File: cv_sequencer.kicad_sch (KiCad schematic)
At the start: 66 parts, among them J1 4005_SWD_Header, J2 3086_Connector_Eurorack_Power, J3 3096_USBC_RA_SMD, SW1 RST, SW2 BOOTSEL, U1 3097_TFT_Display_SPI, U2 4002_RP2040, U3 4015_Adjustable_Reg_500mA_SOT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, U4 4015_Adjustable_Reg_500mA_SOT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, Y1 4004-Crystal-12MHz_GND24

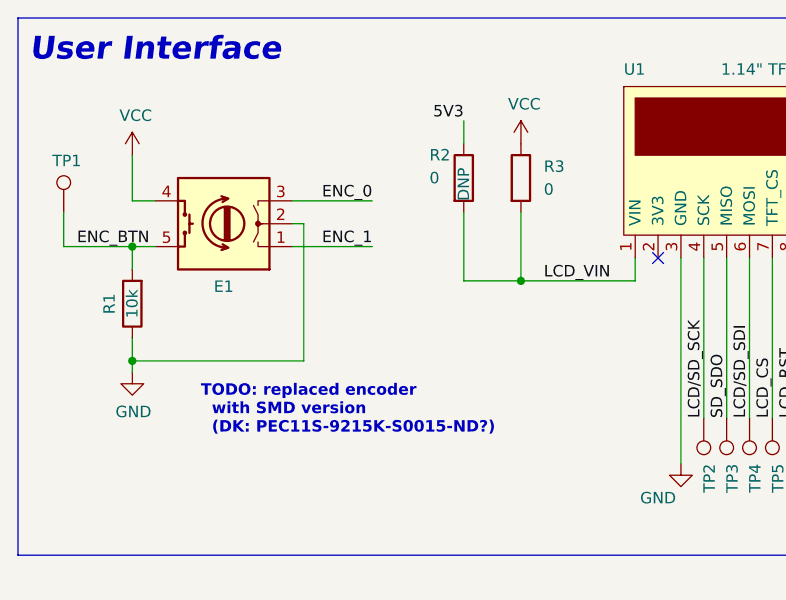
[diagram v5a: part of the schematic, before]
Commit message: Changed encoder to SMD version
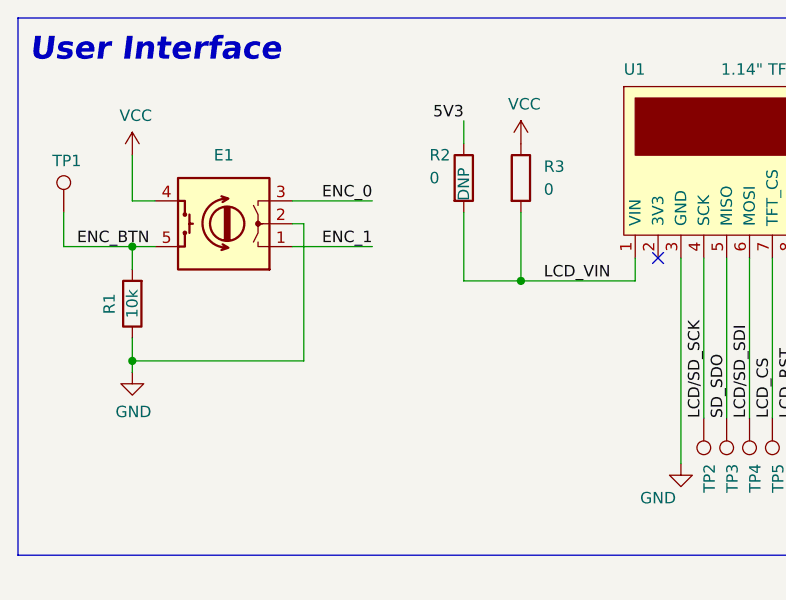
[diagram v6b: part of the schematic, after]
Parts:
- removed E1: 3094_Encoder_Switch, Shulltronics_ElectroMechanical:3094_Encoder_PEC11R, symbol Shulltronics_ElectroMechanical:3094_Encoder_Switch
- added E1: 4025_Encoder_Switch_SMD, Shulltronics_ElectroMechanical:4025_Encoder_PEC11S, symbol Shulltronics_ElectroMechanical:4025_Encoder_Switch_SMD
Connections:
- net ENC_0: now also E1.3
- net ENC_1: now also E1.1
- net ENC_BTN: now also E1.5
- net GND: now also E1.2
- net VCC: now also E1.4
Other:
- note removed: "TODO: replaced encoder with SMD version (DK: PEC11S-9215K-S0015-ND?)"
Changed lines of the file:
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@@
     (effects (font (size 1.27 1.27)) (justify left bottom))
-  )
-  (text "TODO: replaced encoder\n  with SMD version\n  (DK: PEC11S-9215K-S0015-ND?)"
-    (at 34.29 60.325 0)
-    (effects (font (size 1.27 1.27) (thickness 0.254) bold) (justify left bottom))
   )
   (text "USB and SWD Connectors" (at 212.09 90.17 0)
@@
     (pin "5")
   )
+  (symbol (lib_id "Shulltronics_ElectroMechanical:4025_Encoder_Switch_SMD") (at 36.83 36.83 180) (unit 1)
+    (in_bom yes) (on_board yes) (fields_autoplaced)
+    (property "Reference" "E1" (id 0) (at 36.83 29.21 0))
+    (property "Value" "4025_Encoder_Switch_SMD" (id 1) (at 36.83 30.48 0)
+      (effects (font (size 1.27 1.27)) hide)
+    )
+    (property "Footprint" "Shulltronics_ElectroMechanical:4025_Encoder_PEC11S" (id 2) (at 36.83 36.83 0)
+      (effects (font (size 1.27 1.27)) hide)
+    )
+    (property "Datasheet" "https://www.bourns.com/docs/Product-Datasheets/PEC11S.pdf" (id 3) (at 36.83 36.83 0)
+      (effects (font (size 1.27 1.27)) hide)
+    )
+    (property "SPN" "4025" (id 4) (at 36.83 27.94 0)
+      (effects (font (size 1.27 1.27)) hide)
+    )
+    (pin "1")
+    (pin "2")
+    (pin "3")
+    (pin "4")
+    (pin "5")
+  )
   (symbol (lib_id "Shulltronics_Passives:3089_Capacitor_100n_16V_0402") (at 210.82 39.37 90) (unit 1)
     (in_bom yes) (on_board yes)
@@
     (pin "1")
     (pin "2")
-  )
-  (symbol (lib_id "Shulltronics_ElectroMechanical:3094_Encoder_Switch") (at 36.83 36.83 180) (unit 1)
-    (in_bom yes) (on_board yes)
-    (property "Reference" "E1" (id 0) (at 36.83 43.815 0))
-    (property "Value" "3094_Encoder_Switch" (id 1) (at 36.83 30.48 0)
-      (effects (font (size 1.27 1.27)) hide)
-    )
-    (property "Footprint" "Shulltronics_ElectroMechanical:3094_Encoder_PEC11R" (id 2) (at 36.83 36.83 0)
-      (effects (font (size 1.27 1.27)) hide)
-    )
-    (property "Datasheet" "https://www.bourns.com/docs/Product-Datasheets/PEC11R.pdf" (id 3) (at 36.83 36.83 0)
-      (effects (font (size 1.27 1.27)) hide)
-    )
-    (property "SPN" "3094" (id 4) (at 36.83 27.94 0)
-      (effects (font (size 1.27 1.27)) hide)
-    )
-    (pin "1")
-    (pin "2")
-    (pin "3")
-    (pin "4")
-    (pin "5")
   )
   (symbol (lib_id "Shulltronics_Passives:3089_Capacitor_100n_16V_0402") (at 135.89 105.41 0) (unit 1)
@@
       (reference "C26") (unit 1) (value "3089_Capacitor_100n_16V_SMD") (footprint "Shulltronics_Generics:C_0402_HandSolder")
     )
-    (path "/77f076a8-329e-4a40-96ea-5854a454e032"
-      (reference "E1") (unit 1) (value "3094_Encoder_Switch") (footprint "Shulltronics_ElectroMechanical:3094_Encoder_PEC11R")
+    (path "/16a49ecd-abfd-4d6b-abb3-2f90d5cb3b16"
+      (reference "E1") (unit 1) (value "4025_Encoder_Switch_SMD") (footprint "Shulltronics_ElectroMechanical:4025_Encoder_PEC11S")
     )
     (path "/66b30126-0f41-4f28-aeb6-68976a864457"

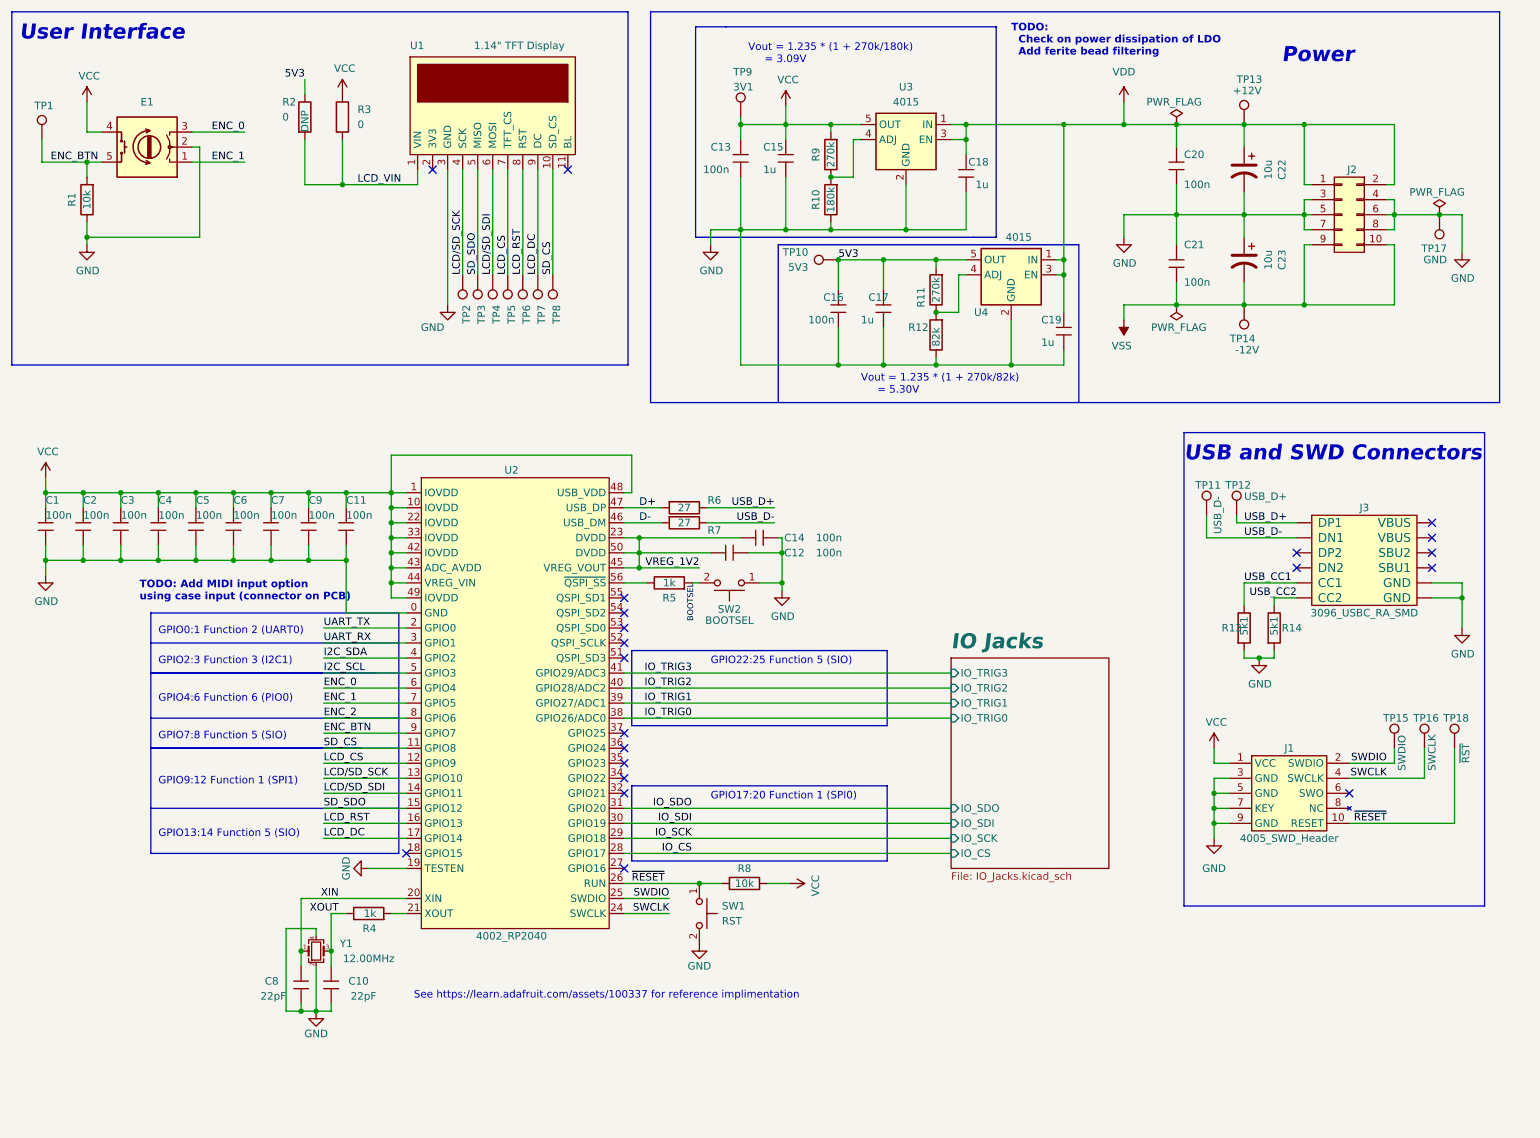
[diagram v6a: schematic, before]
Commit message: gots most components placed nicely, added 4027 for MIDI, still to finish
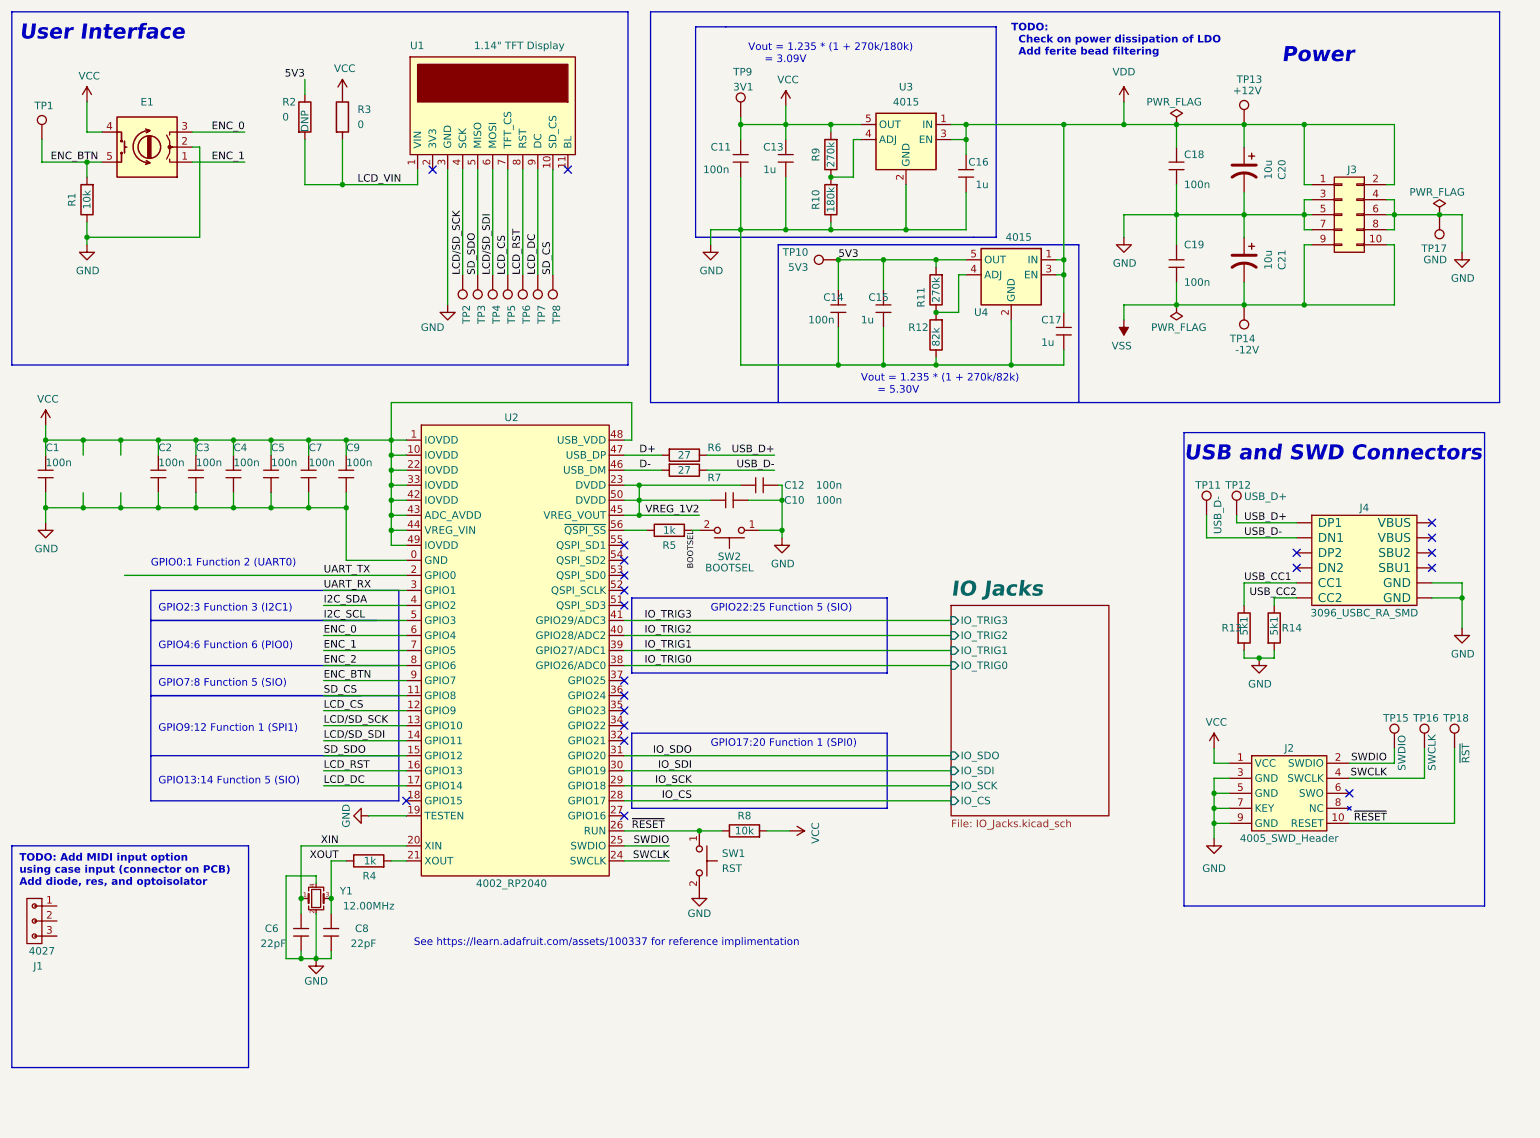
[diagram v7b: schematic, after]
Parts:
- removed C2, C3: 3089_Capacitor_100n_16V_0402, Shulltronics_Generics:C_0402_HandSolder, symbol Shulltronics_Passives:3089_Capacitor_100n_16V_0402
- added J1: 4027_Connector_PicoBlade_3pos_Vert_THT, Shulltronics_Connectors:4027_PicoBlade_3pos_Vert_THT, symbol Shulltronics_Connectors:4027_Connector_PicoBlade_3pos_Vert_THT
- renumbered C12 to C10, C13 to C11, C14 to C12, C15 to C13, C16 to C14, C17 to C15, C18 to C16, C19 to C17, C20 to C18, C21 to C19, C4 to C2, C22 to C20, C23 to C21, C5 to C3, C6 to C4, C7 to C5, C8 to C6, C9 to C7, C10 to C8, C11 to C9, J1 to J2, J2 to J3, J3 to J4
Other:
- note added: "TODO: Add MIDI input option using case input (connector on PCB) Add diode, res, and optoisolator"
- note removed: "TODO: Add MIDI input option using case input (connector on PCB)"
- moved on the sheet: C1, C10, C12, C2, C3, C4, C5, C6, C7, C8, C9, R4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

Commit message: Made minor tweaks, started routing of board
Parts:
- removed C13, C15, C16, C17: 4013_Capacitor_1u_16V_0402, Shulltronics_Generics:C_0402_HandSolder, symbol Shulltronics_Passives:4013_Capacitor_1u_16V_0402
- removed C20, C21: 3088_Capacitor_10u_50V_SMD, Shulltronics_Passives:3088_Capacitor_10u_50V_SMD, symbol Shulltronics_Passives:3088_Capacitor_10u_50V_SMD
- removed J1: 4027_Connector_PicoBlade_3pos_Vert_THT, Shulltronics_Connectors:4027_PicoBlade_3pos_Vert_THT, symbol Shulltronics_Connectors:4027_Connector_PicoBlade_3pos_Vert_THT
- removed R10: 4020_Resistor_SMD_180k_0.125W_1%, Shulltronics_Generics:RES-0402, symbol Shulltronics_Passives:4020_Resistor_SMD_180k_0.125W_1%
- removed R11, R9: 4019_Resistor_SMD_270k_0.125W_1%, Shulltronics_Generics:RES-0402, symbol Shulltronics_Passives:4019_Resistor_SMD_270k_0.125W_1%
- removed R12: 4018_Resistor_SMD_82k_0.125W_1%, Shulltronics_Generics:RES-0402, symbol Shulltronics_Passives:4018_Resistor_SMD_82k_0.125W_1%
- removed U3, U4: 4015_Adjustable_Reg_500mA_SOT-23-5, Shulltronics_Generics:SOT-23-5, symbol Shulltronics_Regulators:4015_Adjustable_Reg_500mA_SOT-23-5
- added C13, C15, C16, C17: 4035_Capacitor_2u2_25V_0402, Shulltronics_Generics:C_0402_HandSolder, symbol Shulltronics_Passives:4035_Capacitor_2u2_25V_0402
- added C20, C21: 4031_Capacitor_10u_35V_SMD, Shulltronics_Passives:3088_Capacitor_10u_50V_SMD, symbol Shulltronics_Passives:4031_Capacitor_10u_35V_SMD
- added J1: 4029_Connector_PicoBlade_4pos_Vert_THT, Shulltronics_Connectors:4029_PicoBlade_4pos_Vert_THT, symbol Shulltronics_Connectors:4029_Connector_PicoBlade_4pos_Vert_THT
- added R10: 4033_Resistor_SMD_18k_0.125W_1%, Shulltronics_Generics:RES-0402, symbol Shulltronics_Passives:4033_Resistor_SMD_18k_0.125W_1%
- added R11, R9: 4016_Resistor_SMD_27k_0.125W_1%, Shulltronics_Generics:RES-0402, symbol Shulltronics_Passives:4016_Resistor_SMD_27k_0.125W_1%
- added R12: 4034_Resistor_SMD_8k2_0.125W_1%, Shulltronics_Generics:RES-0402, symbol Shulltronics_Passives:4034_Resistor_SMD_8k2_0.125W_1%
- added R31, R33: 4030_Resistor_SMD_220_0.125W_1%, Shulltronics_Generics:RES-0402, symbol Shulltronics_Passives:4030_Resistor_SMD_220_0.125W_1%
- added R32: 4008_Resistor_SMD_10k_0.125W_1%, Shulltronics_Generics:RES-0402, symbol Shulltronics_Passives:4008_Resistor_SMD_10k_0.125W_1%
- added U3, U4: 4032_Adjustable_Reg_200mA_SOT-23-5, Shulltronics_Generics:SOT-23-5, symbol Shulltronics_Regulators:4032_Adjustable_Reg_200mA_SOT-23-5
- added U9: 4028_OptoIsolator_TLP290, Shulltronics_Opto:4028_OptoIsolator_TLP290_SOP-4, symbol Shulltronics_Opto:4028_OptoIsolator_TLP290
- J2: SPN (none) -> 4005
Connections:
- net 5V3: now also C15.2, R11.1, U4.5 (OUT)
- net GND: now also C13.1, C15.1, C16.1, C17.1, C20.2, C21.1, R10.2, R12.2, U3.2 (GND), U4.2 (GND), U9.3
- net UART_RX: now also R32.2, U9.4
- net UART_TX: now also J1.3
- net VCC: now also C13.2, R32.1, R33.2, R9.1, U3.5 (OUT)
- net VDD: now also C16.2, C17.2, C20.1, U3.1 (IN), U3.3 (EN), U4.1 (IN), U4.3 (EN)
- net VSS: now also C21.2
- net XOUT: now also R4.2, U2.21 (XOUT); no longer C8.2, R4.1, Y1.3
- new net: R11.2, R12.1, U4.4 (ADJ)
- new net: C8.2, R4.1, Y1.3
- new net: R10.1, R9.2, U3.4 (ADJ)
- new net MIDI_OUT_SRC: J1.4, R33.1
- new net MIDI_R: R31.1, U9.2
- new net MIDI_SNK: J1.1, R31.2
- new net MIDI_SRC: J1.2, U9.1
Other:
- sheet IO Jacks ports: added IO_5V3; removed none
- note added: "MIDI IO"
- note added: "See https://learn.adafruit.com/assets/100337 for RP2040 reference implimentation"
- note added: "TODO: Add PWR and STAT LEDs"
- note added: "TODO: Check on power dissipation of regulator Add ferite bead filtering"
- note added: "TODO: Do I need external pull-ups on the encoder? [X] - I don't think so."
- note added: "Vout = 1.2 * (1 + 27k/18k) = 3.0V"
- note added: "Vout = 1.2 * (1 + 27k/8k2) = 5.15V"
- note removed: "See https://learn.adafruit.com/assets/100337 for reference implimentation"
- note removed: "TODO: Add MIDI input option using case input (connector on PCB) Add diode, res, and optoisolator"
- note removed: "TODO: Check on power dissipation of LDO Add ferite bead filtering"
- note removed: "Vout = 1.235 * (1 + 270k/180k) = 3.09V"
- note removed: "Vout = 1.235 * (1 + 270k/82k) = 5.30V"
- moved on the sheet: C1, C6, C8, R4, Y1
